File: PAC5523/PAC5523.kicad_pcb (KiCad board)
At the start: 2 copper layers, 60 x 50 mm, 126 parts, among them J1 W, J10 NTC, J11 LED, J2 U, J3 V, J4 GND, J5 VIN, J6 UART, J7 SWD, J8 HALL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

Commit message: wip
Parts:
- removed JP1, JP3: UART/RS485, Jumper:SolderJumper-3_P1.3mm_Bridged2Bar12_Pad1.0x1.5mm
- removed JP4: HALL_V, Jumper:SolderJumper-3_P1.3mm_Bridged2Bar12_Pad1.0x1.5mm
- removed R20: 120, Resistor_SMD:R_0603_1608Metric
- removed R37: 1k, Resistor_SMD:R_0603_1608Metric
- removed R38: 100, Resistor_SMD:R_0603_1608Metric
- added R45: 100, Resistor_SMD:R_0603_1608Metric, F.Cu at (111.4, 104.8)
- added R46: 1k, Resistor_SMD:R_0603_1608Metric, F.Cu at (111.4, 107.3)
- added R47: 1k, Resistor_SMD:R_0603_1608Metric, F.Cu at (111.4, 109.8)
- D1, D10, D11, D12, D13, D14, D15, D16, D17, D2, D3, D4, D5, D6, D7, D8, D9: footprint Diode_SMD:D_SMA -> Diode_SMD:D_SOD-123F
- J9: value CAN -> LED
- JP2: footprint Jumper:SolderJumper-3_P1.3mm_Bridged2Bar12_Pad1.0x1.5mm -> Jumper:SolderJumper-3_P1.3mm_Open_Pad1.0x1.5mm_NumberLabels
- R14: footprint Resistor_SMD:R_2512_6332Metric -> Resistor_SMD:R_0805_2012Metric
- U4: footprint Package_SO:SOIC-16W_5.3x10.2mm_P1.27mm -> Package_SO:SOIC-16_3.9x9.9mm_P1.27mm
- moved R29 165.4 mm to (22.9, 31.3), turned to 270 degrees
- moved U8 164.6 mm to (26.4, 34.8)
- moved J10 161.1 mm to (64.3, 26.1), turned to 180 degrees
- moved J7 155.0 mm to (17.2, 37.4), turned to 180 degrees
- moved U7 153.6 mm to (13.2, 32.3)
- moved J11 151.8 mm to (74.5, 26.1), turned to 180 degrees
- moved R27 148.9 mm to (28.7, 31.3), turned to 270 degrees
- moved J8 146.2 mm to (26.6, 26.1), turned to 180 degrees
- moved R33 145.3 mm to (24.3, 31.3), turned to 90 degrees
- moved R34 142.3 mm to (27.2, 31.3), turned to 90 degrees
- moved JP2 142.2 mm to (169.8, 31.4)
- moved R35 140.3 mm to (30.2, 31.3), turned to 90 degrees
- moved R28 140.1 mm to (25.8, 31.3), turned to 270 degrees
- moved C6 127.6 mm to (30.6, 34.7), turned to 180 degrees
- moved C7 125.0 mm to (30.6, 36.1), turned to 180 degrees
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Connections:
- C26 pad 1: 3V3 -> +5V
- J8 pad 1: Net-(J8-Pad1) -> VIO
- J9 pad 1: CANL -> VIO
- J9 pad 3: CANH -> Net-(J9-Pad3)
- R33 pad 1: +5V -> VIO
- R33 pad 2: HALL3 -> Net-(J8-Pad4)
- R34 pad 1: +5V -> VIO
- R34 pad 2: HALL2 -> Net-(J8-Pad3)
- R35 pad 1: +5V -> VIO
- R35 pad 2: HALL1 -> Net-(J8-Pad2)
- R4 pad 2: UART_RX -> CANTX
- R5 pad 2: UART_TX -> CANRX
- U1 pad 36: HALL3 -> HALL1
- U1 pad 37: HALL1 -> HALL2
- U1 pad 38: HALL2 -> HALL3
- U6 pad 1: UART_TX -> CANRX
- U6 pad 4: UART_RX -> CANTX
- U7 pad 1: Net-(U7-Pad1) -> NTC
- U7 pad 4: NTC -> SWDIO
- U7 pad 6: Ain -> SWDCL
- U8 pad 4: HALL2 -> HALL1
- U8 pad 6: HALL1 -> HALL2
- U9 pad 1: UART_RX -> CANRX
- U9 pad 3: UART_TX -> CANTX
- U9 pad 4: SWDIO -> Net-(U9-Pad4)
- U9 pad 6: SWDCL -> Ain
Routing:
- net CANL: track 0.00 -> 14.1 mm
- net CANRX: track 0.00 -> 14.1 mm
- net CANH: track 0.00 -> 11.2 mm
- net CANTX: track 0.00 -> 4.88 mm
- net RS485RXTX: track 0.00 -> 1.27 mm
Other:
- board size 60 x 50 mm -> 60 x 44 mm
- copper layers 2 -> 4
- board text added: "Trafo Multi Footprint https://static6.arrow.com/aropdfconversion/99173437d2dd4c695891522b71595793bc5862a8/p847.pdf"

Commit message: wip
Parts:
- removed J7: SWD, Connector_PinHeader_2.54mm:PinHeader_1x04_P2.54mm_Vertical
- removed R21, R22: 100, Resistor_SMD:R_0603_1608Metric
- added P1: TC2030-CTX-Tag-Connect, otter:TC2030, F.Cu at (22.3, 37.1)
- U5: footprint Package_TO_SOT_SMD:SOT-23-5 -> Package_TO_SOT_SMD:SOT-353_SC-70-5
- moved C38 126.0 mm to (69.2, 35.7), turned to 270 degrees
- moved C35 125.3 mm to (63.1, 41.5), turned to 270 degrees
- moved C36 122.0 mm to (68.5, 38.0), turned to 180 degrees
- moved L1 120.1 mm to (64.8, 36.4), turned to 90 degrees
- moved D17 119.6 mm to (65.0, 40.9), turned to 270 degrees
- moved R42 116.1 mm to (72.3, 39.5), turned to 180 degrees
- moved R41 115.6 mm to (73.1, 37.2), turned to 270 degrees
- moved C37 112.5 mm to (71.1, 36.4), turned to 270 degrees
- moved U2 108.8 mm to (68.1, 40.5)
- moved JP2 108.6 mm to (64.8, 59.0)
- moved U7 14.5 mm to (26.4, 38.4)
- moved C1 1.10 mm to (35.5, 28.9)
- moved C11 1.10 mm to (39.6, 28.9)
- moved D1 1.10 mm to (36.5, 25.7)
- moved D2 1.10 mm to (34.4, 25.7)
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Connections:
- U7 pad 1: NTC -> SWDIO
- U7 pad 3: Net-(U7-Pad3) -> SWDCL
- U7 pad 4: SWDIO -> NTC
- U7 pad 6: SWDCL -> Net-(U7-Pad6)
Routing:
- net SWDCL: track 0.00 -> 3.69 mm
- net SWDIO: track 0.00 -> 3.04 mm

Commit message: wip
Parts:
- removed R32: 1k, Resistor_SMD:R_0603_1608Metric
- added C39: 100p, Capacitor_SMD:C_0603_1608Metric, F.Cu at (141.1, 43.9)
- added C40: 100p, Capacitor_SMD:C_0603_1608Metric, F.Cu at (145.6, 39.4)
- added C41: 18p, Capacitor_SMD:C_0603_1608Metric, F.Cu at (115.8, 54.4)
- added D18: SS310, Diode_SMD:D_SOD-123F, F.Cu at (136.4, 39.8)
- added D19: SS310, Diode_SMD:D_SOD-123F, F.Cu at (136.4, 43.1)
- added D20: SK6812MINI, LED_SMD:LED_SK6812MINI_PLCC4_3.5x3.5mm_P1.75mm, F.Cu at (112.7, 47.1)
- added Q2: Q_NMOS_GSD, Package_TO_SOT_SMD:SOT-23, F.Cu at (141.3, 40.4)
- added R20: 47k, Resistor_SMD:R_0603_1608Metric, F.Cu at (145.6, 41.9)
- added R21: 1M, Resistor_SMD:R_0603_1608Metric, F.Cu at (145.1, 44.4)
- added U11: ENCODER B, Package_SO:SOIC-8_3.9x4.9mm_P1.27mm, F.Cu at (122.0, 41.3)
- U4: value AM26LS32 -> Oscillator_3225; footprint Package_SO:SOIC-16_3.9x9.9mm_P1.27mm -> otter:Oscillator_3225
- U5: value NL17SZ125 -> ENCODER A; footprint Package_TO_SOT_SMD:SOT-353_SC-70-5 -> Package_SO:SOIC-8_3.9x4.9mm_P1.27mm
- moved U4 100.0 mm to (111.5, 55.0)
- moved U5 40.2 mm to (113.5, 41.3), turned to 0 degrees
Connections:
- J10 pad 1: GND -> NTC_EXT_GND
- J10 pad 2: Net-(J10-Pad2) -> NTC_EXT
- R39 pad 1: NTC_EXT -> NTC_IO
- R39 pad 2: Net-(J10-Pad2) -> NTC_EXT
- R43 pad 1: NTC -> NTC_EXT
- U1 pad 1: Net-(U1-Pad1) -> ENC_B
- U1 pad 2: SWDIO -> ENC_A
- U1 pad 45: NTC -> NTC_IO
- U1 pad 46: NTC_EXT -> SWDIO
- U4 pad 1: ENC_A_B -> Net-(U4-Pad1)
- U4 pad 2: ENC_A_A -> GND
- U4 pad 3: ENC_A -> CLK
- U4 pad 4: Net-(U4-Pad4) -> VIO
- U5 pad 1: GND -> Net-(U5-Pad1)
- U5 pad 2: SK6812 -> GND
- U5 pad 4: SK6812_OUT -> ENC_A
- U5 pad 5: +5V -> GND
- U7 pad 4: NTC -> NTC_EXT

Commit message: placement almost done
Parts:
- removed D18: SS310, Diode_SMD:D_SOD-123F
- removed R17, R18, R6: TBD, Resistor_SMD:R_0603_1608Metric
- removed R43: 100, Resistor_SMD:R_0603_1608Metric
- removed R44, R47: 1k, Resistor_SMD:R_0603_1608Metric
- added J7: ENCODER, Connector_Molex:Molex_PicoBlade_53261-0671_1x06-1MP_P1.25mm_Horizontal, F.Cu at (39.9, 26.1)
- J9: value LED -> AIN
- JP2: value HALL_V -> UART
- R1: footprint Resistor_SMD:R_0805_2012Metric -> Resistor_SMD:R_0603_1608Metric
- moved C34 186.6 mm to (32.2, 31.3), turned to 270 degrees
- moved R30 133.5 mm to (46.3, 29.3), turned to 270 degrees
- moved R25 130.3 mm to (47.5, 36.9)
- moved R26 128.9 mm to (50.4, 36.8)
- moved R31 128.7 mm to (44.6, 32.3), turned to 270 degrees
- moved R24 122.7 mm to (46.5, 47.3), turned to 90 degrees
- moved C31 121.4 mm to (58.6, 35.4), turned to 180 degrees
- moved R23 121.3 mm to (46.5, 50.2), turned to 90 degrees
- moved C10 120.8 mm to (44.5, 29.4), turned to 270 degrees
- moved C29 119.4 mm to (60.9, 32.9), turned to 90 degrees
- moved R39 116.6 mm to (69.3, 33.0), turned to 90 degrees
- moved C30 116.1 mm to (58.6, 34.0), turned to 180 degrees
- moved R7 103.6 mm to (58.6, 36.9), turned to 180 degrees
- moved C17 103.2 mm to (62.3, 32.9), turned to 270 degrees
- moved C18 102.0 mm to (63.8, 32.9), turned to 90 degrees
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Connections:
- C24 pad 1: VIO -> +5V
- D19 pad 2: Net-(D18-Pad1) -> NTC_EXT
- J5 pad 1: Net-(J5-Pad1) -> NTC_EXT
- J8 pad 1: VIO -> +5V
- J9 pad 2: GND -> Net-(J9-Pad2)
- J9 pad 3: Net-(J9-Pad3) -> GND
- R20 pad 1: VIO -> 3V3
- R45 pad 2: Net-(J9-Pad3) -> Net-(J9-Pad2)
- R46 pad 1: 3V3 -> VIO
- R46 pad 2: Net-(J9-Pad3) -> Net-(J9-Pad2)
- U7 pad 4: NTC_EXT -> Net-(U7-Pad4)
- U7 pad 6: Net-(U7-Pad6) -> NTC_EXT
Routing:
- net CANTX: track 4.88 -> 15.4 mm
- net CLK: track 0.00 -> 7.98 mm
- net NTC_EXT: track 0.00 -> 7.31 mm
- net CANH: track 11.2 -> 18.3 mm
- net NTC_IO: track 0.00 -> 4.58 mm
- net VIO: track 0.00 -> 4.32 mm
- net SWDIO: track 3.04 -> 7.08 mm
- net CANL: track 14.1 -> 18.0 mm
- net SWDCL: track 3.69 -> 0.52 mm
- net VCC18: track 0.00 -> 2.84 mm
- net VCORE: track 0.00 -> 2.70 mm
- net Vin_mon: track 0.00 -> 1.87 mm
- net CANRX: track 14.1 -> 15.3 mm
- added copper zone on B.Cu, net GND
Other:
- net class Default: clearance 0.2 -> 0.154; trace_width 0.25 -> 0.2; via_dia 0.8 -> 0.6; via_drill 0.4 -> 0.3
- rule trace_clearance: 0.2 -> 0.154
- rule trace_min: 0.2 -> 0.154

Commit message: routing 60% done
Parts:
- moved C34 3.22 mm to (34.6, 29.1), turned to 0 degrees
- moved C26 1.11 mm to (74.7, 58.3)
- moved C1 0.95 mm to (66.2, 43.5)
- moved U11 0.49 mm to (36.2, 33.8)
- moved U5 0.49 mm to (41.6, 33.8)
- moved R31 0.45 mm to (45.0, 32.4)
- moved R14 0.30 mm to (47.0, 58.5)
- moved Q1 0.29 mm to (51.0, 63.0)
- moved D2 0.28 mm to (67.9, 46.6)
- moved R1 0.20 mm to (50.3, 57.5)
- moved P1 0.16 mm to (78.0, 38.0)
- moved C10 0.16 mm to (44.7, 29.4)
- moved D1 0.15 mm to (65.9, 46.6)
- moved C32 0.10 mm to (46.8, 60.1)
- moved D7 0.08 mm to (63.9, 46.6)
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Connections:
- C20 pad 2: GNDPWR -> GND
- C21 pad 2: GNDPWR -> GND
- C22 pad 2: GNDPWR -> GND
- C23 pad 2: GNDPWR -> GND
- C25 pad 2: GNDPWR -> GND
- C33 pad 2: GNDPWR -> GND
- R14 pad 2: GNDPWR -> GND
- R45 pad 1: AIN -> Ain
- U10 pad 10: GNDPWR -> GND
- U10 pad 9: GNDPWR -> GND
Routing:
- net VP: track 0.00 -> 79.4 mm, vias 0 -> 3
- net GND: track 0.00 -> 56.1 mm, vias 0 -> 71
- net VHM: track 0.00 -> 54.5 mm, vias 0 -> 2
- net +5V: track 0.00 -> 47.5 mm
- net Net-(C20-Pad1): track 0.00 -> 33.8 mm
- net VIO: track 4.32 -> 33.7 mm, vias 0 -> 3
- net Net-(D16-Pad2): track 0.00 -> 27.9 mm
- net SK6812: track 0.00 -> 24.9 mm, vias 0 -> 2
- net DRM: track 0.00 -> 24.9 mm, vias 0 -> 2
- net IWH: track 0.00 -> 18.0 mm, vias 0 -> 1
- net DRL0: track 0.00 -> 17.6 mm
- net IWL: track 0.00 -> 16.9 mm, vias 0 -> 1
- net DRL1: track 0.00 -> 16.6 mm
- net DRL2: track 0.00 -> 15.4 mm
- net SWDCL: track 0.52 -> 15.9 mm, vias 0 -> 2
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- added copper zone on F.Cu, net GND

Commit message: finalized board, silkscreen needs some work
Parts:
- removed C27, C4: 100n, Capacitor_SMD:C_0603_1608Metric
- added C42: 100p, Capacitor_SMD:C_0603_1608Metric, F.Cu at (21.2, 63.9)
- added R17: 4k3, Resistor_SMD:R_0603_1608Metric, F.Cu at (22.5, 63.9)
- added R6: 100k, Resistor_SMD:R_0603_1608Metric, F.Cu at (21.7, 58.6)
- moved U8 4.02 mm to (31.6, 31.1)
- moved R29 1.15 mm to (21.7, 31.3)
- moved R33 1.15 mm to (23.2, 31.3)
- moved R35 1.15 mm to (29.0, 31.3)
- moved R27 1.15 mm to (27.6, 31.3)
- moved R28 1.15 mm to (24.6, 31.3)
- moved R34 1.15 mm to (26.1, 31.3)
- moved C29 0.68 mm to (60.6, 32.3)
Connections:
- U8 pad 1: HALL3 -> HALL2
- U8 pad 3: Net-(U8-Pad3) -> HALL3
- U8 pad 4: HALL1 -> Net-(U8-Pad4)
- U8 pad 6: HALL2 -> HALL1
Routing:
- net +5V: track 47.5 -> 161.8 mm, vias 0 -> 6
- net Vin_mon: track 1.87 -> 99.7 mm, vias 0 -> 2
- net VIO: track 33.7 -> 105.1 mm, vias 3 -> 5
- net HALL3: track 10.6 -> 70.8 mm, vias 1 -> 2
- net HALL2: track 7.07 -> 67.3 mm, vias 1 -> 2
- net NTC_EXT: track 13.9 -> 72.8 mm, vias 0 -> 1
- net HALL1: track 5.67 -> 60.7 mm, vias 1 -> 2
- net ENC_B: track 0.00 -> 54.4 mm, vias 0 -> 4
- net ENC_A: track 0.00 -> 49.3 mm, vias 0 -> 4
- net CSM: track 8.78 -> 44.9 mm, vias 1 -> 2
- net UU: track 2.79 -> 35.5 mm, vias 0 -> 2
- net IUL: track 5.01 -> 31.5 mm, vias 0 -> 2
- net IUH: track 2.07 -> 27.2 mm, vias 0 -> 2
- net DRS3: track 6.61 -> 31.0 mm, vias 0 -> 2
- net DRS5: track 4.79 -> 26.7 mm, vias 0 -> 2
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- added copper zone on F.Cu, net +5V
- added copper zone on In2.Cu, net GND
- added copper zone on F.Cu, net Net-(C36-Pad2)
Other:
- board text removed: "Trafo Multi Footprint https://static6.arrow.com/aropdfconversion/99173437d2dd4c695891522b71595793bc5862a8/p847.pdf"

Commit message: finalized silkscreen
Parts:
- JP2: footprint Jumper:SolderJumper-3_P1.3mm_Open_Pad1.0x1.5mm_NumberLabels -> Jumper:SolderJumper-3_P1.3mm_Open_RoundedPad1.0x1.5mm
- moved R45 0.58 mm to (59.6, 57.3)
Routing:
- net GND: track 72.1 -> 74.7 mm, vias 91 -> 92
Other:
- board text added: "3.3V"
- board text added: "5V"

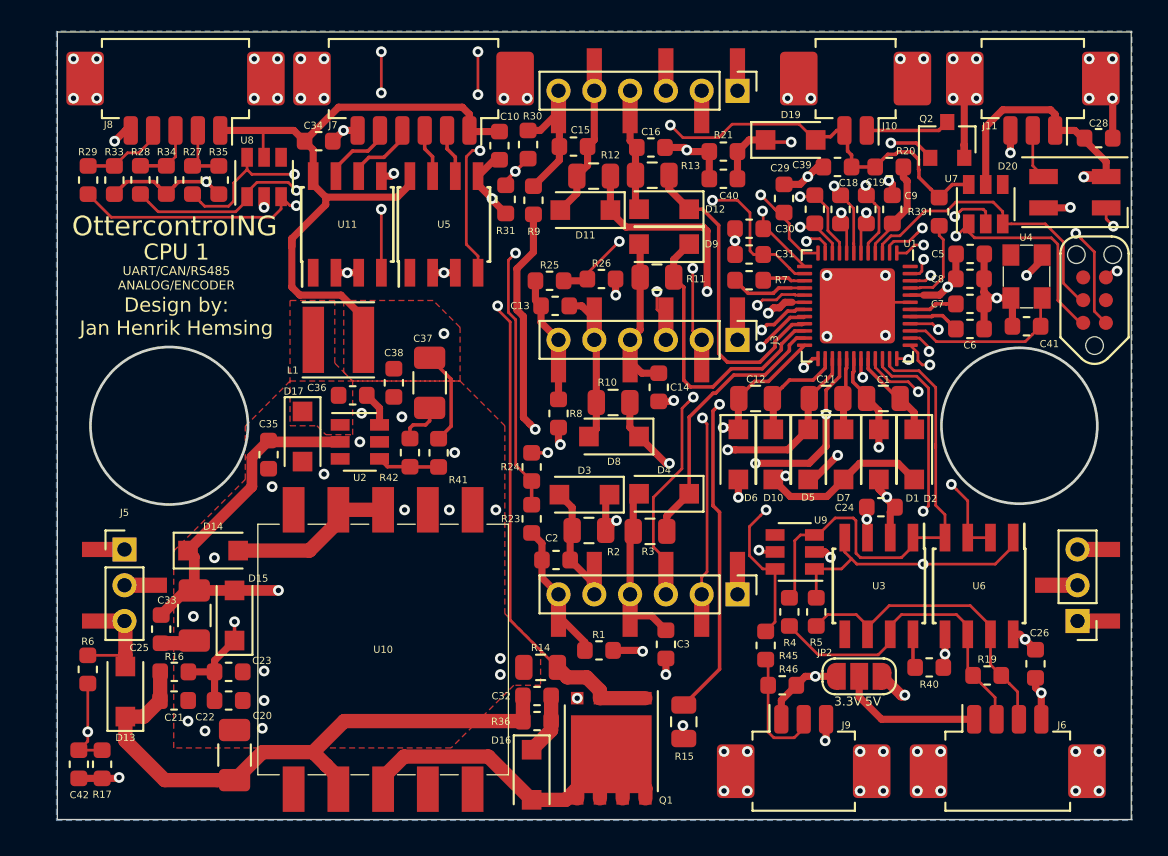
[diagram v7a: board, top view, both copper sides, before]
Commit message: finalized silkscreen, generated gerber
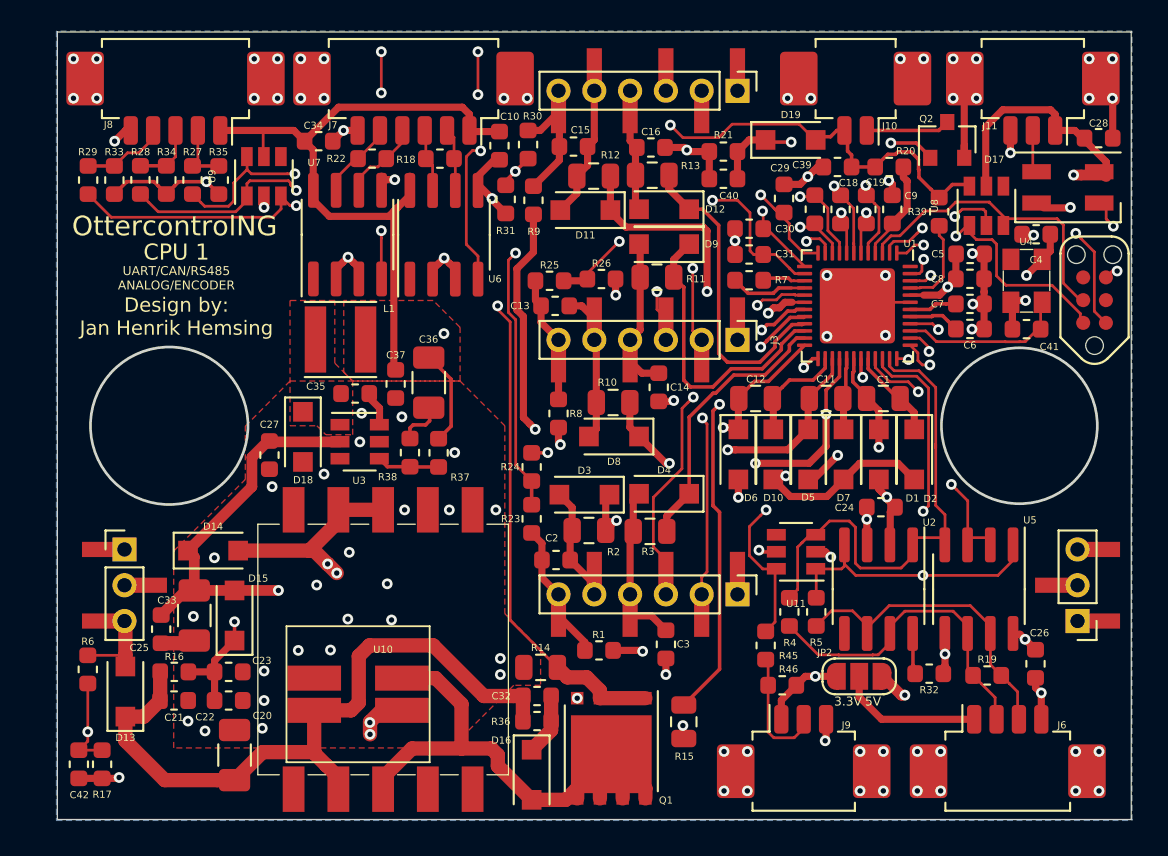
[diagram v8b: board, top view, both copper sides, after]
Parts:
- removed C38: 100n, Capacitor_SMD:C_0603_1608Metric
- removed D20: SK6812MINI, LED_SMD:LED_SK6812MINI_PLCC4_3.5x3.5mm_P1.75mm
- removed R40: 4k3, Resistor_SMD:R_0603_1608Metric
- removed R41: 100k, Resistor_SMD:R_0603_1608Metric
- removed R42: 19k3, Resistor_SMD:R_0603_1608Metric
- added C27: 100n, Capacitor_SMD:C_0603_1608Metric, F.Cu at (31.9, 46.6)
- added C4: 100n, Capacitor_SMD:C_0603_1608Metric, F.Cu at (74.7, 34.3)
- added D18: SS310, Diode_SMD:D_SOD-123F, F.Cu at (33.7, 45.6)
- added R18: 120, Resistor_SMD:R_0603_1608Metric, F.Cu at (41.4, 30.1)
- added R22: 120, Resistor_SMD:R_0603_1608Metric, F.Cu at (37.6, 30.1)
- added R32: 4k3, Resistor_SMD:R_0603_1608Metric, F.Cu at (68.7, 58.9)
- added R37: 47k, Resistor_SMD:R_0603_1608Metric, F.Cu at (41.3, 46.5)
- added R38: 9k6, Resistor_SMD:R_0603_1608Metric, F.Cu at (39.7, 46.5)
- C36: value 100n -> 10u; footprint Capacitor_SMD:C_0603_1608Metric -> Capacitor_SMD:C_1206_3216Metric
- C37: value 10u -> 100n; footprint Capacitor_SMD:C_1206_3216Metric -> Capacitor_SMD:C_0603_1608Metric
- D17: value SS310 -> SK6812MINI; footprint Diode_SMD:D_SOD-123F -> LED_SMD:LED_SK6812MINI_PLCC4_3.5x3.5mm_P1.75mm
- U11: value ENCODER B -> USBLC6-4; footprint Package_SO:SOIC-8_3.9x4.9mm_P1.27mm -> Package_TO_SOT_SMD:SOT-23-6
- U2: value ACT4088 -> MAX3051; footprint Package_TO_SOT_SMD:SOT-23-6 -> Package_SO:SOIC-8_3.9x4.9mm_P1.27mm
- U3: value MAX3051 -> ACT4088; footprint Package_SO:SOIC-8_3.9x4.9mm_P1.27mm -> Package_TO_SOT_SMD:SOT-23-6
- U5: value ENCODER A -> RS485
- U6: value RS485 -> ENCODER A
- U7: value USBLC6-4 -> ENCODER B; footprint Package_TO_SOT_SMD:SOT-23-6 -> Package_SO:SOIC-8_3.9x4.9mm_P1.27mm
- moved D17 45.0 mm to (76.5, 31.7), turned to 0 degrees
- moved U8 40.4 mm to (71.9, 32.7)
- moved U9 36.3 mm to (31.5, 31.1), turned to 90 degrees
- moved U5 36.2 mm to (71.5, 54.1), turned to 270 degrees
- moved U6 35.8 mm to (41.6, 34.3), turned to 90 degrees
- moved U7 35.7 mm to (36.2, 34.3)
- moved U11 31.0 mm to (61.3, 52.0), turned to 180 degrees
- moved U2 30.1 mm to (65.9, 54.1), turned to 270 degrees
- moved U3 30.1 mm to (36.9, 45.9), turned to 0 degrees
- moved C35 5.92 mm to (36.6, 43.2), turned to 180 degrees
- moved C36 4.31 mm to (40.8, 42.6), turned to 270 degrees
- moved C37 1.90 mm to (38.9, 42.7)
- moved U4 0.24 mm to (74.2, 36.9)
- moved C41 0.16 mm to (74.2, 39.6)
- moved L1 0.12 mm to (35.8, 40.2)
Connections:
- C35 pad 1: VP -> Net-(C35-Pad1)
- C35 pad 2: GND -> Net-(C35-Pad2)
- C36 pad 1: Net-(C36-Pad1) -> +5V
- C36 pad 2: Net-(C36-Pad2) -> GND
- D17 pad 1: Net-(C36-Pad2) -> SK6812_OUT
- L1 pad 1: Net-(C36-Pad2) -> Net-(C35-Pad2)
- U11 pad 1: Net-(U11-Pad1) -> CANRX
- U11 pad 3: GND -> CANTX
- U11 pad 4: ENC_B -> Net-(U11-Pad4)
- U11 pad 5: GND -> +5V
- U11 pad 6: ENC_B_A -> Ain
- U2 pad 1: Net-(C36-Pad2) -> CANTX
- U2 pad 2: VP -> GND
- U2 pad 3: Net-(U2-Pad3) -> +5V
- U2 pad 4: Net-(R41-Pad2) -> CANRX
- U2 pad 5: GND -> Net-(U2-Pad5)
- U2 pad 6: Net-(C36-Pad1) -> CANL
- U3 pad 1: CANTX -> Net-(C35-Pad2)
- U3 pad 2: GND -> VP
- U3 pad 3: +5V -> Net-(U3-Pad3)
- U3 pad 4: CANRX -> Net-(R37-Pad2)
- U3 pad 5: Net-(U3-Pad5) -> GND
- U3 pad 6: CANL -> Net-(C35-Pad1)
- U5 pad 1: Net-(U5-Pad1) -> CANRX
- U5 pad 2: GND -> RS485RXTX
- U5 pad 3: GND -> RS485RXTX
- U5 pad 4: ENC_A -> CANTX
- U5 pad 6: ENC_A_A -> CANH
- U5 pad 7: ENC_A_B -> CANL
- U6 pad 1: CANRX -> Net-(U6-Pad1)
- U6 pad 2: RS485RXTX -> GND
- U6 pad 3: RS485RXTX -> GND
- U6 pad 4: CANTX -> ENC_A
- U6 pad 6: CANH -> ENC_A_A
- U6 pad 7: CANL -> ENC_A_B
- U7 pad 1: SWDIO -> Net-(U7-Pad1)
- U7 pad 3: SWDCL -> GND
- U7 pad 4: Net-(U7-Pad4) -> ENC_B
- U7 pad 5: +5V -> GND
- U7 pad 6: NTC_EXT -> ENC_B_A
- U8 pad 1: HALL2 -> SWDIO
- U8 pad 3: HALL3 -> SWDCL
- U8 pad 6: HALL1 -> NTC_EXT
- U9 pad 1: CANRX -> HALL2
- U9 pad 3: CANTX -> HALL3
- U9 pad 6: Ain -> HALL1
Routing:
- net Net-(D14-Pad2): track 9.43 -> 24.7 mm, vias 0 -> 4
- net Net-(D16-Pad2): track 27.9 -> 35.1 mm
- net Net-(C20-Pad1): track 33.8 -> 39.6 mm
- net Net-(R41-Pad2): track 3.49 -> 0.00 mm
- net Net-(R37-Pad2): track 0.00 -> 3.49 mm
- net GND: track 74.7 -> 77.8 mm, vias 92 -> 103
- net CANRX: track 29.3 -> 32.0 mm
- net Net-(C36-Pad1): track 1.95 -> 0.00 mm
- net Net-(C35-Pad1): track 0.00 -> 1.95 mm
- net Net-(R40-Pad1): track 1.90 -> 0.00 mm
- net Net-(R32-Pad1): track 0.00 -> 1.90 mm
- net VIO: track 105.1 -> 106.6 mm
- net HALL2: track 67.3 -> 68.5 mm
- net +5V: track 161.8 -> 162.5 mm
- net CANL: track 18.0 -> 17.4 mm
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- added copper zone on F.Cu, net Net-(C35-Pad2)
- removed copper zone on F.Cu, net Net-(C36-Pad2)
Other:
- board text added: "B A"
- board text added: "GND AIN 3.3V"
- board text added: "GND B- B+ A- A+ +5V"
- board text added: "GND CANL CANH VCC"
- board text added: "GND H3 H2 H1 VIO"
- board text added: "GND SK6812 +5V"
- board text added: "NTC"
- board text added: "RX TX"
